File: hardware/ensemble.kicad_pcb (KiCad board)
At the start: 2 copper layers, 50 x 55 mm, 22 parts, among them J1 E1, SW1 4PDT Toggle, SW2 SPDT Toggle, SW3 SPST Toggle, T1 42TM_XX, U1 LM741

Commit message: initial layout
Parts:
- C3: value 2.2u -> 2u2
- moved SW3 64.7 mm to (30.7, 50.3), turned to 90 degrees
- moved SW2 50.6 mm to (30.7, 62.2), turned to -90 degrees
- moved R2 47.8 mm to (32.8, 31.5), turned to 90 degrees
- moved T1 44.7 mm to (42.6, 53.4), turned to -90 degrees
- moved SW1 39.1 mm to (64.0, 50.5), turned to -90 degrees
- moved R1 32.0 mm to (57.1, 31.0)
- moved D1 24.5 mm to (61.4, 41.0), turned to 0 degrees
- moved C3 22.6 mm to (48.5, 25.0), turned to 0 degrees
- moved C1 22.3 mm to (58.5, 28.0), turned to 0 degrees
- moved U1 21.6 mm to (36.4, 24.0)
- moved C2 21.0 mm to (58.5, 25.0), turned to 0 degrees
- moved R4 21.0 mm to (47.2, 31.0), turned to 0 degrees
- moved D2 20.9 mm to (61.4, 43.2), turned to 0 degrees
- moved D4 19.4 mm to (47.9, 43.2), turned to 180 degrees
- moved D3 13.4 mm to (38.1, 43.2), turned to 180 degrees
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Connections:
- SW1 pad 4: /XFM_S3 -> /XFM_P1
- SW1 pad 5: GND -> /RECT_TOP
- SW1 pad 6: /XFM_P3 -> /XFM_S1
- SW1 pad 7: /XFM_P1 -> /XFM_S3
- SW1 pad 8: /RECT_TOP -> GND
- SW1 pad 9: /XFM_S1 -> /XFM_P3

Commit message: add link and revision
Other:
- board text added: "${COMMENT1} ${REVISION}"
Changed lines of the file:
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@@
   (gr_arc (start 73 71) (mid 72.414214 72.414214) (end 71 73)
     (stroke (width 0.1) (type default)) (layer "Edge.Cuts"))
+  (gr_text "     ${COMMENT1}                                     ${REVISION}    " (at 72.75 72.75) (layer "B.SilkS" knockout)
+    (effects (font (size 0.8 0.8) (thickness 0.15)) (justify left bottom mirror))
+  )
   (zone (net 15) (net_name "GND") (layer "B.Cu") (hatch edge 0.5)
     (connect_pads (clearance 0.5))

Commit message: further iteration on layout
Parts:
- moved R2 26.8 mm to (58.4, 23.8), turned to 180 degrees
- moved D4 25.3 mm to (26.3, 30.0), turned to 0 degrees
- moved U1 20.5 mm to (51.8, 37.5), turned to 180 degrees
- moved D3 16.0 mm to (34.1, 27.8)
- moved D5 16.0 mm to (26.4, 25.5)
- moved D1 15.3 mm to (61.9, 25.8)
- moved D2 15.3 mm to (61.9, 28.0)
- moved T1 14.1 mm to (54.5, 61.0), turned to 90 degrees
- moved R1 13.8 mm to (45.4, 23.8), turned to 180 degrees
- moved D6 10.8 mm to (33.9, 32.2), turned to 180 degrees
- moved R4 8.66 mm to (41.0, 37.1), turned to 90 degrees
- moved C2 8.14 mm to (50.6, 26.8), turned to 180 degrees
- moved RV3 7.94 mm to (31.7, 24.1), turned to 0 degrees
- moved RV1 7.87 mm to (64.8, 24.1), turned to 0 degrees
- moved RV2 6.25 mm to (48.0, 38.2)
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
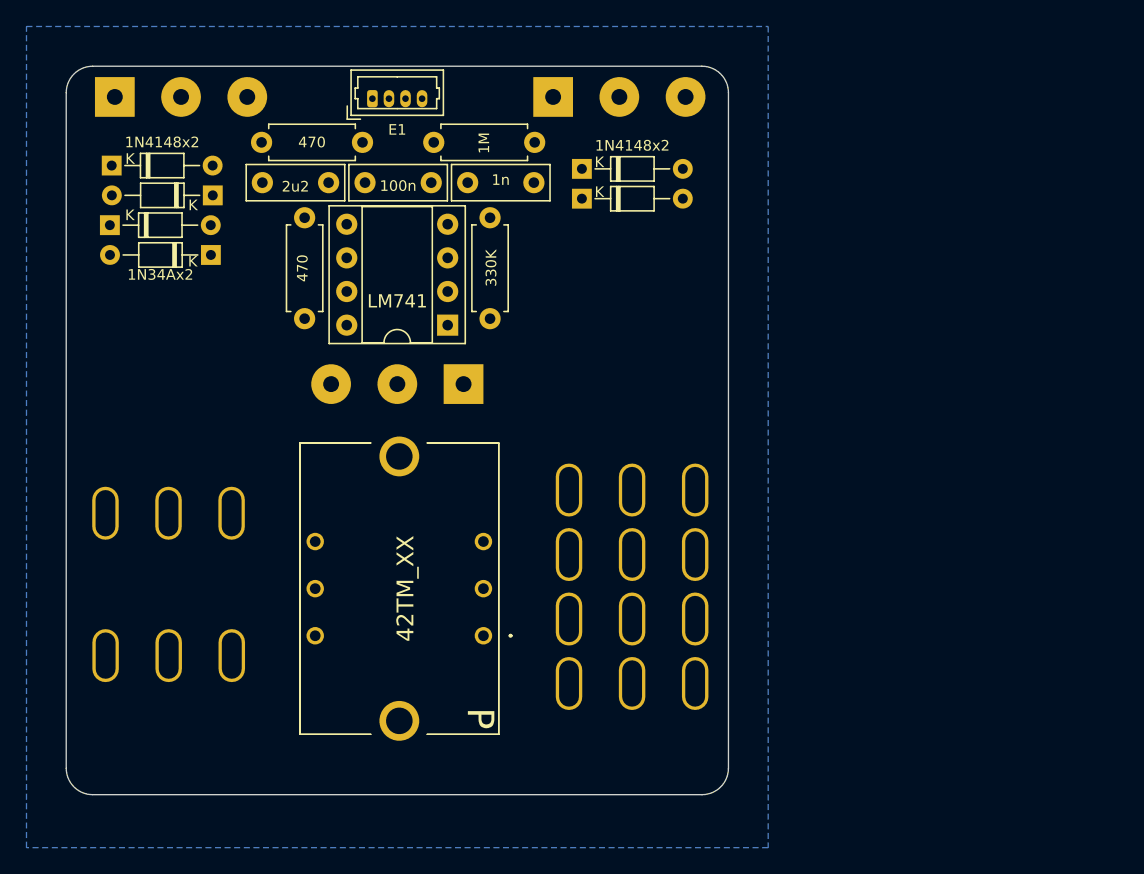
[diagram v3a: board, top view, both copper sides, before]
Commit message: fix 4pdt model alignment and initial routing
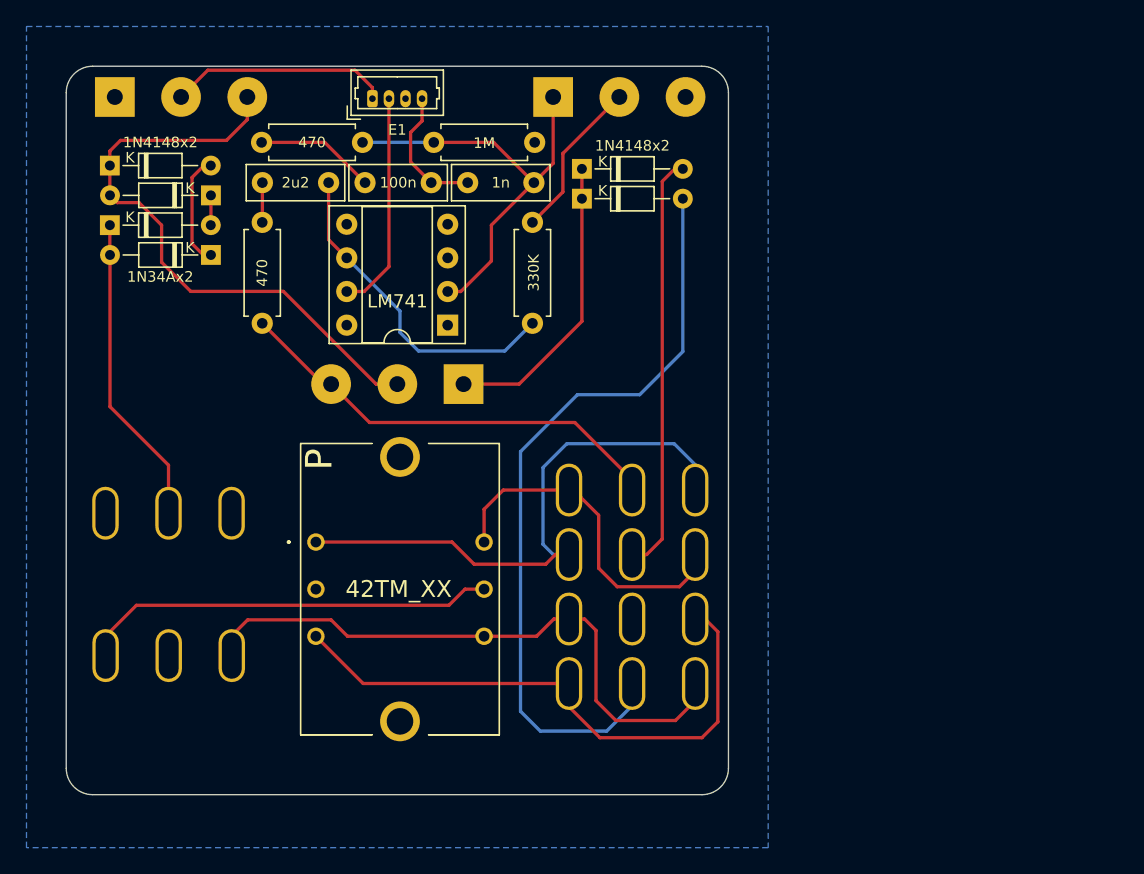
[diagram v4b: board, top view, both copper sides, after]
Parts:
- moved T1 14.5 mm to (41.9, 53.9), turned to -90 degrees
- moved R3 3.22 mm to (58.2, 29.8)
- moved R4 3.22 mm to (37.8, 37.4)
- moved D3 0.14 mm to (33.9, 27.8)
- moved D5 0.14 mm to (26.3, 25.5)
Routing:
- net /RECT_BOTTOM: track 0.00 -> 58.0 mm
- net /XFM_S3: track 0.00 -> 46.2 mm
- net Net-(D3-A): track 0.00 -> 45.7 mm
- net /XFM_P3: track 0.00 -> 44.0 mm
- net /XFM_P1: track 0.00 -> 43.0 mm
- net /DRIVE_OUT: track 0.00 -> 33.6 mm
- net Net-(U1--): track 0.00 -> 32.8 mm
- net /RECT_TOP: track 0.00 -> 31.7 mm
- net /XFM_S2: track 0.00 -> 31.5 mm
- net /XFM_S1: track 0.00 -> 26.1 mm
- net Net-(C3-Pad1): track 0.00 -> 25.0 mm
- net Net-(D4-K): track 0.00 -> 23.6 mm
- net /OCTAVE_OUT: track 0.00 -> 22.4 mm
- net /EFFECT_OUT: track 0.00 -> 16.7 mm
- net /9V0: track 0.00 -> 16.6 mm
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
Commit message: tweak input-side filtering based on simulations, move to correct footprint for caps and diodes.
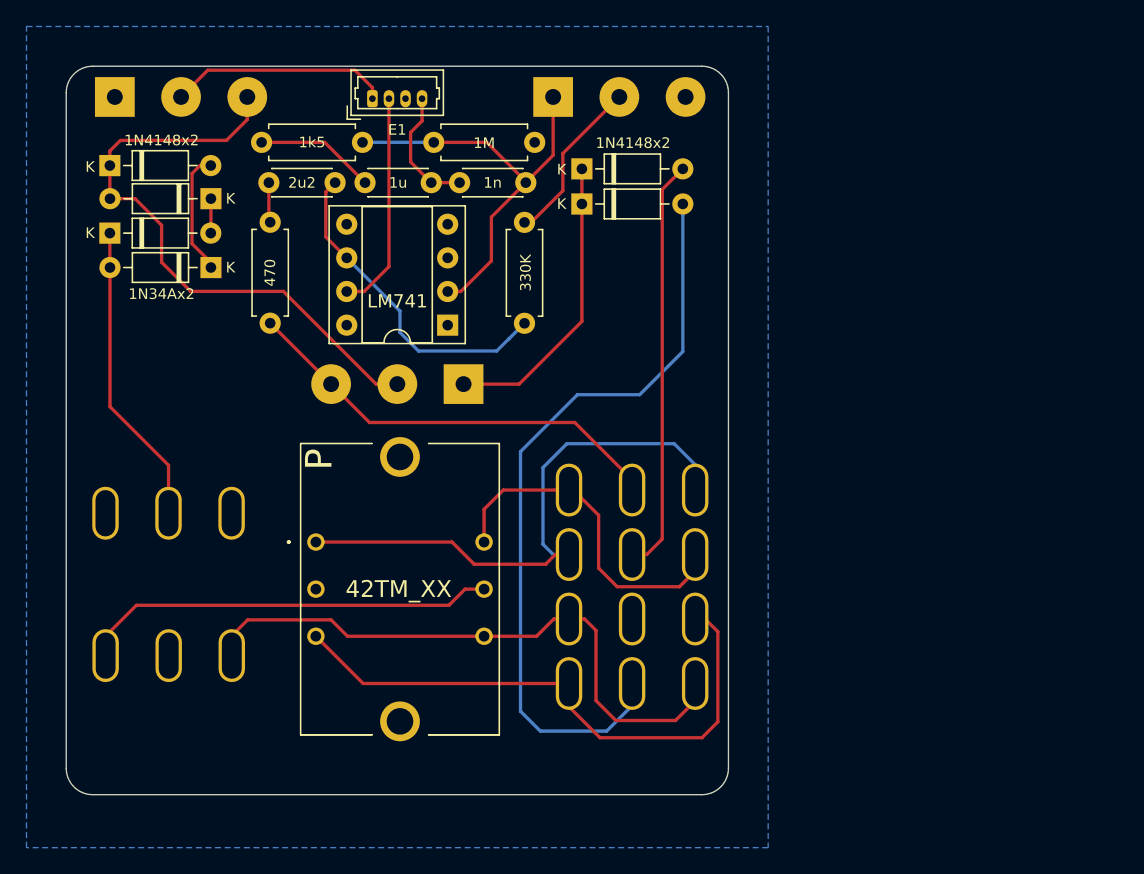
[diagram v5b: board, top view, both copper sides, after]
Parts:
- C1, C3: footprint Capacitor_THT:C_Rect_L7.2mm_W2.5mm_P5.00mm_FKS2_FKP2_MKS2_MKP2 -> Capacitor_THT:C_Disc_D4.3mm_W1.9mm_P5.00mm
- C2: value 100n -> 1u; footprint Capacitor_THT:C_Rect_L7.2mm_W2.5mm_P5.00mm_FKS2_FKP2_MKS2_MKP2 -> Capacitor_THT:C_Disc_D4.3mm_W1.9mm_P5.00mm
- D1, D2, D3, D4, D5, D6: footprint Diode_THT:D_DO-34_SOD68_P7.62mm_Horizontal -> Diode_THT:D_DO-35_SOD27_P7.62mm_Horizontal
- R1: value 470 -> 1k5
- moved D6 0.95 mm to (33.9, 33.2)
- moved C1 0.61 mm to (52.7, 26.8)
- moved R4 0.60 mm to (38.4, 37.4)
- moved D4 0.60 mm to (26.3, 30.6)
- moved R3 0.60 mm to (57.6, 29.8)
- moved C3 0.49 mm to (43.3, 26.8)
- moved D2 0.40 mm to (61.9, 28.4)
- moved D3 0.25 mm to (33.9, 28.0)
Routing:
- net Net-(D5-A): track 8.56 -> 9.35 mm
- net /EFFECT_IN: track 10.1 -> 9.49 mm
- net Net-(D4-K): track 23.6 -> 23.0 mm
- net /DRIVE_OUT: track 33.6 -> 33.0 mm
- net Net-(U1--): track 32.8 -> 32.2 mm
- net Net-(R3-Pad1): track 12.2 -> 12.7 mm

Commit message: slight routing and layout changes
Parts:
- moved D1 6.40 mm to (61.9, 32.1)
- moved D2 6.40 mm to (61.9, 34.8)
- moved D3 4.10 mm to (33.9, 32.1)
- moved D4 4.10 mm to (26.3, 34.7)
- moved D5 4.10 mm to (26.3, 29.6)
- moved D6 4.10 mm to (33.9, 37.3)
- moved SW2 2.40 mm to (30.7, 64.9)
- moved RV3 0.99 mm to (30.8, 24.6)
- moved RV1 0.65 mm to (65.2, 24.6)
- moved SW1 0.27 mm to (64.5, 50.7)
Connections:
- net Net-(C3-Pad1) renamed /741_Out
- net Net-(D3-A) renamed /POST_BALANCE
- net Net-(U1--) renamed /741_Inv
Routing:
- net /RECT_TOP: track 31.4 -> 24.8 mm
- net /OCTAVE_OUT: track 22.4 -> 16.0 mm
- net /RECT_BOTTOM: track 57.6 -> 51.5 mm
- net Net-(D4-K): track 23.0 -> 18.9 mm
- net /POST_BALANCE: track 45.8 -> 42.1 mm
- net /741_Out: track 24.8 -> 22.1 mm
- net /XFM_S3: track 46.2 -> 48.0 mm
- net /XFM_S2: track 31.5 -> 33.0 mm
- net /XFM_S1: track 26.1 -> 27.5 mm
- net /741_Inv: track 32.2 -> 31.1 mm
- net /XFM_P1: track 43.0 -> 42.0 mm
- net Net-(R3-Pad1): track 12.7 -> 13.6 mm
- net /DRIVE_OUT: track 33.0 -> 32.2 mm
